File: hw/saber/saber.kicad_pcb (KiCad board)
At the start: 4 copper layers, 82 x 29.7 mm, 77 parts, among them J1 Screw_Terminal_01x02, J2 Screw_Terminal_01x02, J3 Screw_Terminal_01x12, J4 NUCLEO144ZE-STLINK, Q1 STL120N4F6AG, Q2 SIS413DN-T1-GE3, Q3 SSM3K337R, Q4 STL76DN4LF7AG, Q5 SSM3K337R, Q6 SSM3K337R, Q7 SSM3K337R, SW1 SW, U1 STM32L031F4Px, U2 VNHD7008AY, U3 AZ1117IH-3.3TRG1, U4 MMA8452Q

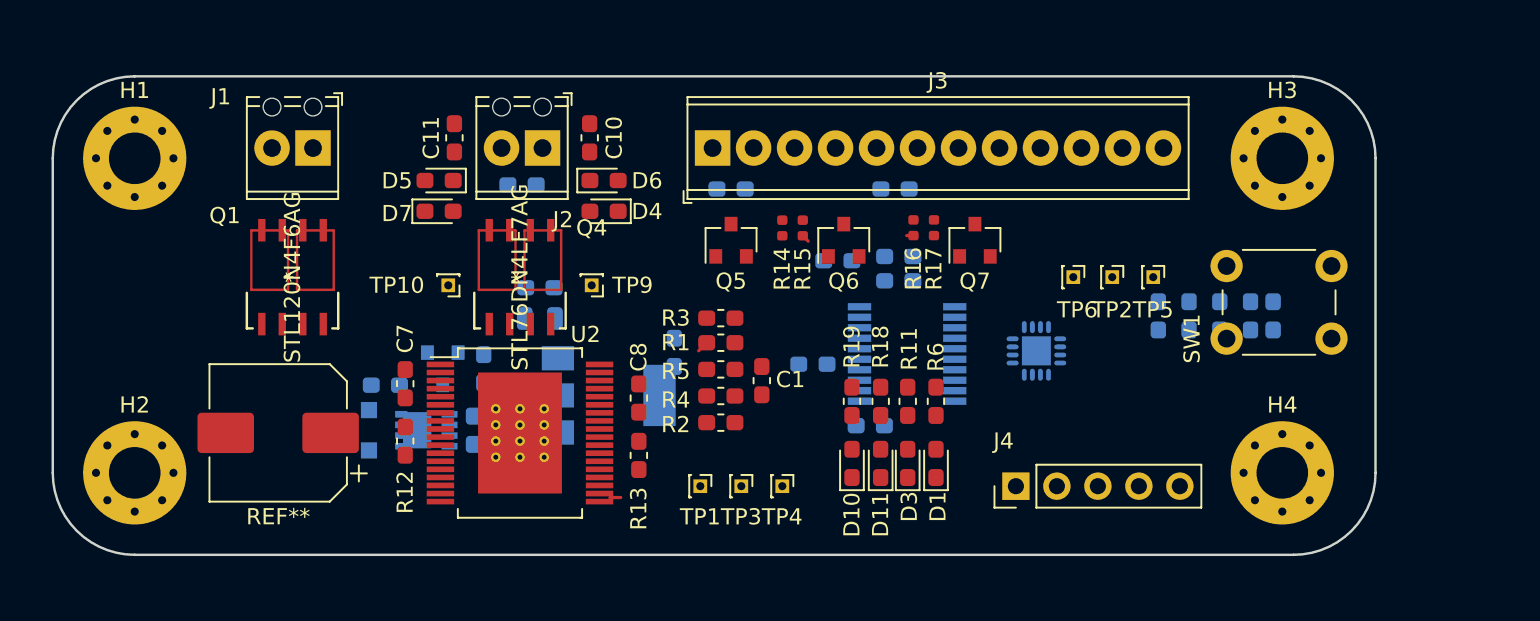
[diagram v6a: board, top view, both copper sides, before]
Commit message: increased density by removing a mounting hole so large cap takes up that corner
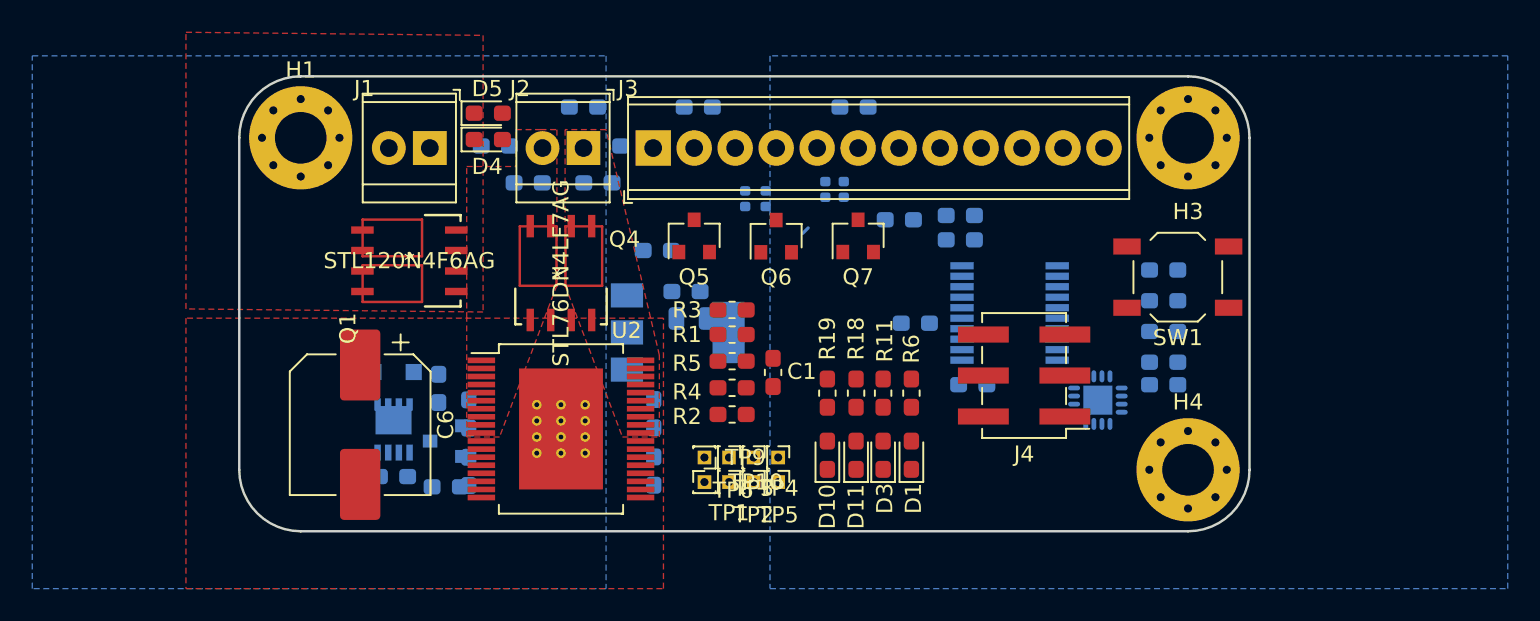
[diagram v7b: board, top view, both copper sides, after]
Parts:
- removed H2: MountingHole_Pad, MountingHole:MountingHole_3.2mm_M3_Pad_Via
- removed REF**: CP_Elec_8x10, Capacitor_SMD:CP_Elec_8x10
- added C6: 200u, Capacitor_SMD:CP_Elec_8x10.5, F.Cu at (121.9, 88.9)
- C10, C11, C7, C8, D6, D7, R12, R13, R14, R15, R16, R17: moved to B.Cu
- J1, J2: value Screw_Terminal_01x02 -> 282834-2; footprint TerminalBlock_Phoenix:TerminalBlock_Phoenix_MPT-0,5-2-2.54_1x02_P2.54mm_Horizontal -> TerminalBlock_TE-Connectivity:TerminalBlock_TE_282834-2_1x02_P2.54mm_Horizontal
- J3: value Screw_Terminal_01x12 -> OSTVN12A150
- J4: footprint Connector_PinHeader_2.54mm:PinHeader_1x05_P2.54mm_Vertical -> Connector_PinHeader_2.54mm:PinHeader_2x03_P2.54mm_Vertical_SMD
- SW1: footprint Button_Switch_THT:SW_PUSH_6mm_H5mm -> Button_Switch_SMD:SW_SPST_TL3342
- moved TP5 26.5 mm to (147.8, 92.5)
- moved TP2 25.6 mm to (146.3, 92.5)
- moved TP6 24.1 mm to (144.8, 90.9)
- moved TP10 20.0 mm to (143.3, 92.5), turned to 0 degrees
- moved TP9 12.8 mm to (143.3, 90.9)
- moved C11 11.2 mm to (138.9, 71.6), turned to 0 degrees
- moved H1 10.4 mm to (118.2, 71.1)
- moved SW1 10.3 mm to (172.6, 79.8)
- moved D7 9.84 mm to (136.7, 73.9), turned to 0 degrees
- moved L1 9.40 mm to (142.5, 82.3)
- moved C12 9.06 mm to (142.1, 80.6)
- moved D4 8.44 mm to (129.9, 71.2), turned to 0 degrees
- moved R20 8.01 mm to (171.7, 86.4), turned to 180 degrees
- moved R10 7.68 mm to (127.3, 92.7), turned to 0 degrees
- moved Q1 7.31 mm to (125.0, 78.7), turned to 180 degrees
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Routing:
- net /hbridge/PWM_MTR: track 0.71 -> 0.00 mm
- net /hbridge/imtr: track 0.68 -> 0.00 mm
- added copper zone on B.Cu, net +12V
- added copper zone on B.Cu, net +3V3
- added copper zone on F.Cu, net /BATT+
- added copper zone on F.Cu, net /MOT+
- added copper zone on F.Cu, net /MOT-
- added copper zone on F.Cu, net /hbridge/VCC
- added copper zone on In2.Cu, net GND
- removed copper zone on In2.Cu, net +12V
- removed copper zone on In2.Cu, net +3V3
- removed copper zone on In2.Cu, net /BATT+
- removed copper zone on In2.Cu, net /hbridge/VCC
- removed copper zone on In1.Cu, net GND
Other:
- board size 82 x 29.7 mm -> 62.6 x 28.2 mm

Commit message: editing layout for density
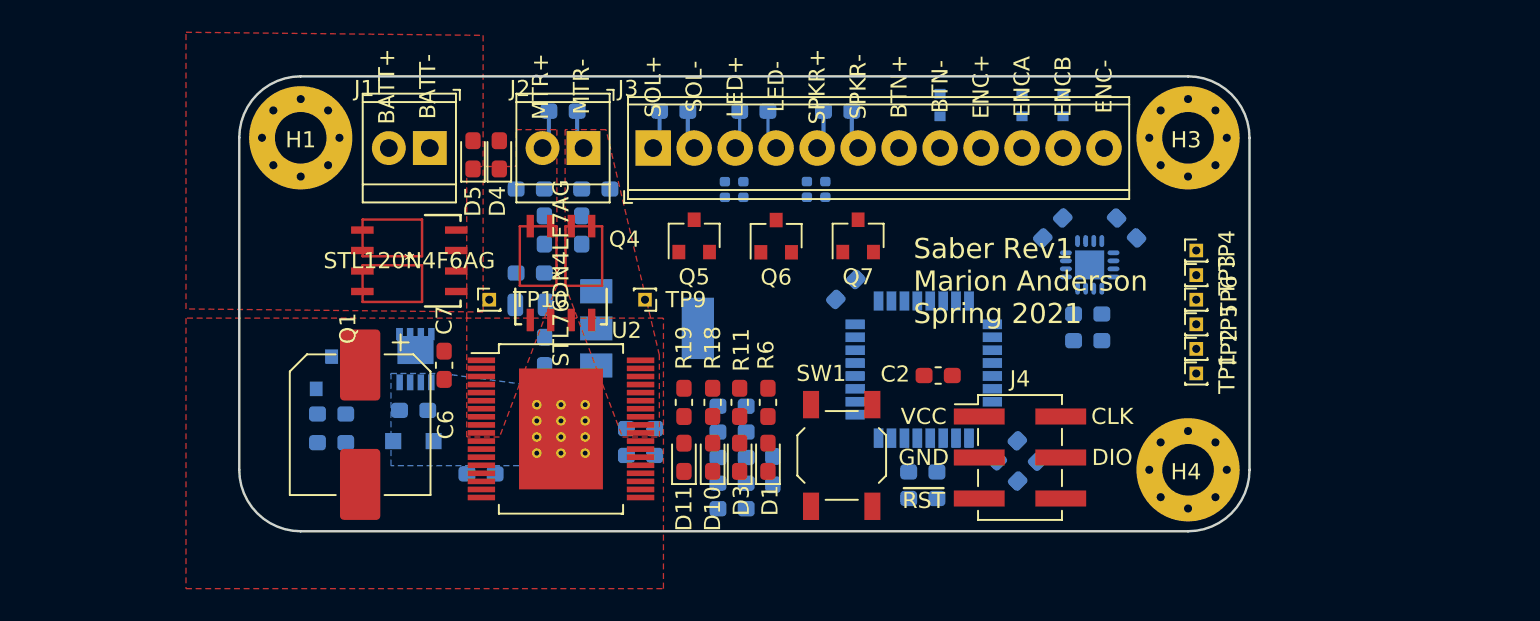
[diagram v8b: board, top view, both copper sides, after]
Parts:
- removed C14: 100n, Capacitor_SMD:C_0603_1608Metric_Pad1.05x0.95mm_HandSolder
- removed R7: 1k, Resistor_SMD:R_0603_1608Metric_Pad1.05x0.95mm_HandSolder
- added C18: 100n, Capacitor_SMD:C_0603_1608Metric_Pad1.05x0.95mm_HandSolder, B.Cu at (156.8, 93.5)
- added C19: 1u, Capacitor_SMD:C_0603_1608Metric_Pad1.05x0.95mm_HandSolder, B.Cu at (156.8, 91.8)
- added D12: SDM2U30CSP-7, Diode_SMD:D_0603_1608Metric_Pad1.05x0.95mm_HandSolder, B.Cu at (146.3, 69.5)
- added D13: BZT585B4V3T-7, Diode_SMD:D_SOD-523, B.Cu at (157.9, 69.1)
- added D14: BZT585B4V3T-7, Diode_SMD:D_SOD-523, B.Cu at (162.9, 69.1)
- added D15: BZT585B4V3T-7, Diode_SMD:D_SOD-523, B.Cu at (165.5, 69.1)
- C1, R1, R2, R3, R4, R5: moved to B.Cu
- C2, C7: moved to F.Cu
- U1: value STM32L031F4Px -> STM32L051K8Tx; footprint Package_SO:TSSOP-20_4.4x6.5mm_P0.65mm -> Package_QFP:LQFP-32_7x7mm_P0.8mm
- moved TP6 30.6 mm to (173.7, 81.2), turned to 0 degrees
- moved TP1 29.7 mm to (173.7, 85.7), turned to 0 degrees
- moved TP3 29.7 mm to (173.7, 79.6), turned to 0 degrees
- moved TP4 28.9 mm to (173.7, 78.1), turned to 0 degrees
- moved TP2 28.6 mm to (173.7, 84.2), turned to 0 degrees
- moved TP5 27.7 mm to (173.7, 82.7), turned to 0 degrees
- moved SW1 23.6 mm to (151.8, 90.8), turned to 270 degrees
- moved TP10 17.5 mm to (129.9, 81.2)
- moved C4 16.4 mm to (163.3, 91.8), turned to 225 degrees
- moved R20 11.9 mm to (164.8, 76.7), turned to 225 degrees
- moved D11 10.7 mm to (142.0, 90.9)
- moved TP9 10.4 mm to (139.6, 81.2)
- moved L1 10.0 mm to (132.5, 81.5)
- moved C12 9.72 mm to (132.5, 79.5)
- moved C13 9.37 mm to (133.3, 84.4), turned to 270 degrees
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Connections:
- C3 pad 1: /micro/BOOT0 -> +3V3
- Q2 pad 1: Net-(Q2-Pad1) -> /hbridge/VCC
- Q2 pad 2: +12V -> /hbridge/VCC
- Q2 pad 4: (no net) -> Net-(Q2-Pad4)
- Q2 pad 5: (no net) -> +12V
- Q3 pad 3: Net-(Q2-Pad1) -> Net-(Q2-Pad4)
- R11 pad 1: Net-(Q2-Pad1) -> Net-(Q2-Pad4)
- R8 pad 2: Net-(Q2-Pad1) -> Net-(Q2-Pad4)
- U1 pad 1: /micro/BOOT0 -> +3V3
- U1 pad 11: /micro/LED_HBEAT -> /micro/PWM_MTR_MCU
- U1 pad 12: /ENC_B -> /micro/INB_MCU
- U1 pad 13: /ENC_A -> Net-(U1-Pad13)
- U1 pad 14: /BTN -> Net-(U1-Pad14)
- U1 pad 15: GND -> Net-(U1-Pad15)
- U1 pad 16: +3V3 -> GND
- U1 pad 17: /acc/SCL -> +3V3
- U1 pad 18: /acc/SDA -> /actuators/SIG_SOL
- U1 pad 19: /micro/SWDIO -> /actuators/SIG_LED
- U1 pad 2: /actuators/SIG_LED -> Net-(U1-Pad2)
- U1 pad 20: /micro/SWCLK -> Net-(U1-Pad20)
- U1 pad 3: /actuators/SIG_SOL -> Net-(U1-Pad3)
- U1 pad 6: /actuators/PWM_SPKR -> Net-(U1-Pad6)
- U1 pad 7: /micro/PWM_MTR_MCU -> Net-(U1-Pad7)
- U1 pad 8: /micro/INA_MCU -> Net-(U1-Pad8)
- U1 pad 9: /micro/INB_MCU -> /micro/INA_MCU
- U4 pad 11: /acc/SCL -> Net-(U4-Pad11)
- U4 pad 2: Net-(R20-Pad1) -> Net-(C17-Pad2)
- U4 pad 4: Net-(U4-Pad4) -> /acc/SCL
- U4 pad 6: Net-(U4-Pad6) -> /acc/SDA
- U4 pad 7: Net-(C17-Pad2) -> Net-(R20-Pad1)
- U4 pad 9: /acc/SDA -> Net-(U4-Pad9)
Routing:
- net /SPKR+: track 0.00 -> 4.07 mm
- net /LED+: track 0.47 -> 4.02 mm
- net /MOT-: track 0.00 -> 2.97 mm
- net /MOT+: track 0.00 -> 2.61 mm
- net /LED-: track 0.00 -> 2.50 mm
- net /SPKR-: track 0.00 -> 2.45 mm
- net /SOL-: track 0.00 -> 2.45 mm
- net +12V: track 0.00 -> 2.45 mm
- net /ENC_B: track 0.00 -> 1.02 mm
- added copper zone on In1.Cu, net +12V
- added copper zone on In1.Cu, net +3V3
- added copper zone on B.Cu, net /hbridge/VCC
- removed copper zone on B.Cu, net +12V
- removed copper zone on B.Cu, net +3V3
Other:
- board text added: "BATT+"
- board text added: "BATT-"
- board text added: "BTN+"
- board text added: "BTN-"
- board text added: "CLK"
- board text added: "DIO"
- board text added: "ENC+"
- board text added: "ENC-"
- board text added: "ENCA"
- board text added: "ENCB"
- board text added: "GND"
- board text added: "LED+"
- board text added: "LED-"
- board text added: "MTR+"
- board text added: "MTR-"
- board text added: "SOL+"
- board text added: "SOL-"
- board text added: "SPKR+"
- board text added: "SPKR-"
- board text added: "Saber Rev1 Marion Anderson Spring 2021"
- board text added: "VCC"
- board text added: "~RST"
